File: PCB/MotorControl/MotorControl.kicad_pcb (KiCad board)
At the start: 2 copper layers, 44 x 54.5 mm, 14 parts, among them J1 USB_C_Receptacle_USB2.0_14P, J2 Conn_02x05_Top_Bottom, J3 Conn_01x06, J4 Conn_01x03, SW1 SW_Push, U1 STM32L031K6Tx, U2 TC1262-33

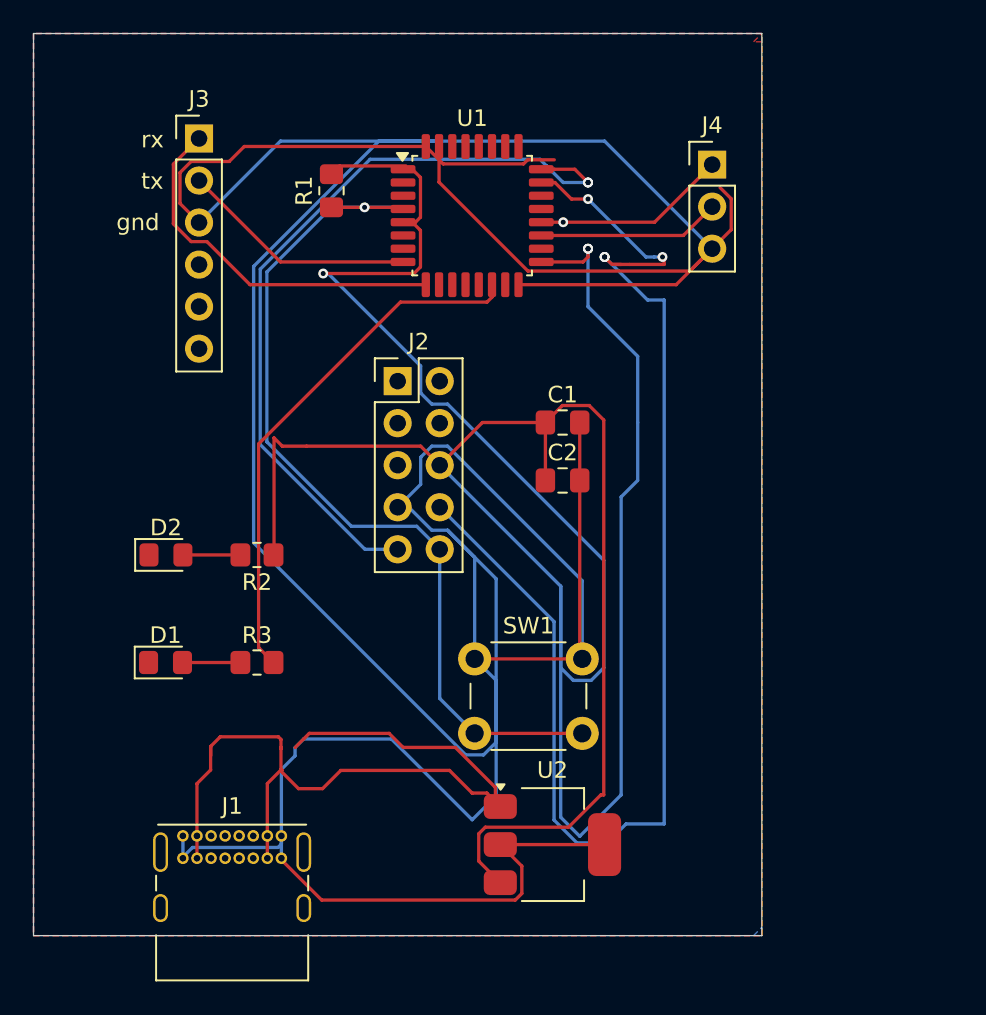
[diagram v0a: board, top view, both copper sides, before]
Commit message: Routing for motor control PCB
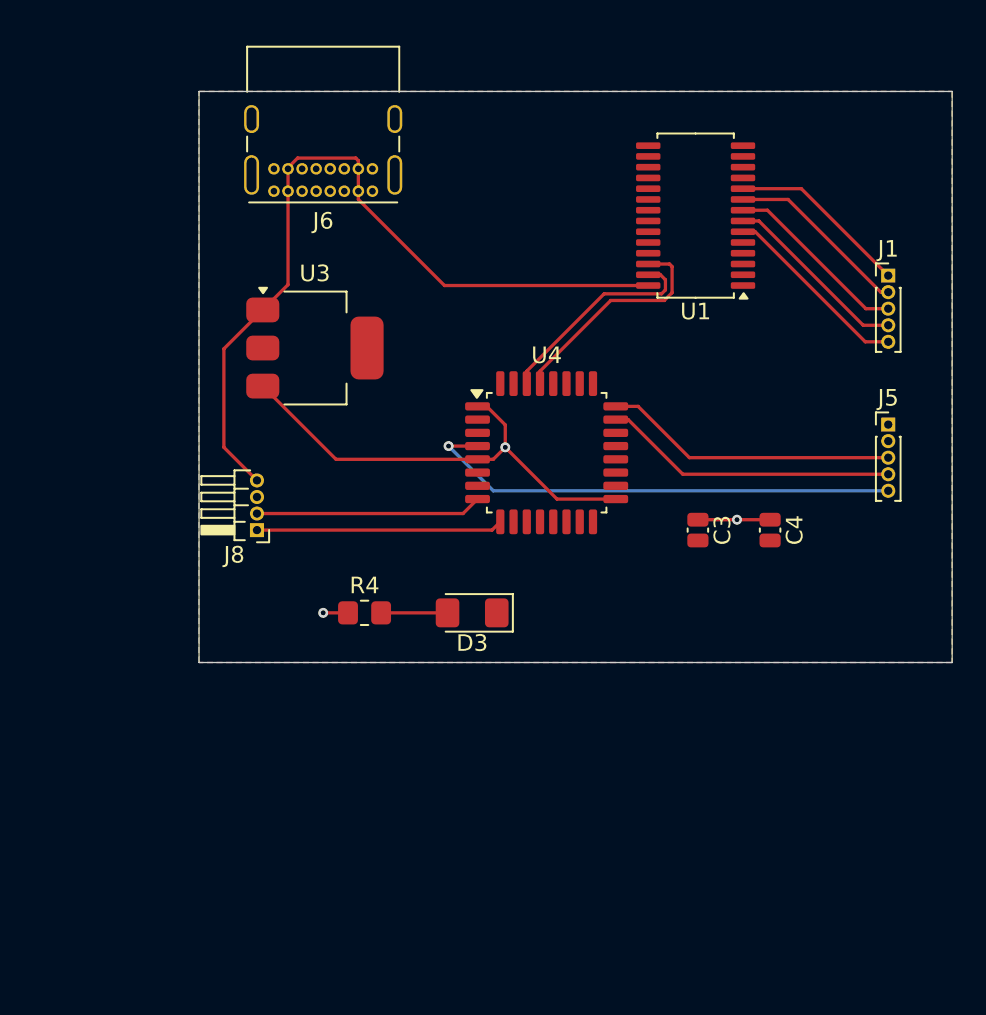
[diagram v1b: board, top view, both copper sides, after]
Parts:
- removed C1: .1uf, Capacitor_SMD:C_0805_2012Metric_Pad1.18x1.45mm_HandSolder
- removed C2: 10uf, Capacitor_SMD:C_0805_2012Metric_Pad1.18x1.45mm_HandSolder
- removed D1, D2: LED, LED_SMD:LED_0805_2012Metric_Pad1.15x1.40mm_HandSolder
- removed J2: Conn_02x05_Top_Bottom, Connector_PinHeader_2.54mm:PinHeader_2x05_P2.54mm_Vertical
- removed J3: Conn_01x06, Connector_PinHeader_2.54mm:PinHeader_1x06_P2.54mm_Vertical
- removed J4: Conn_01x03, Connector_PinHeader_2.54mm:PinHeader_1x03_P2.54mm_Vertical
- removed R1: 4.7k, Resistor_SMD:R_0805_2012Metric_Pad1.20x1.40mm_HandSolder
- removed R2, R3: 330, Resistor_SMD:R_0805_2012Metric_Pad1.20x1.40mm_HandSolder
- removed SW1: SW_Push, Button_Switch_THT:SW_PUSH_6mm_H4.3mm
- removed U2: TC1262-33, Package_TO_SOT_SMD:SOT-223-3_TabPin2
- added C3: 1, Capacitor_SMD:C_0504_1310Metric_Pad0.83x1.28mm_HandSolder, F.Cu at (64.6, 59.0)
- added C4: .1u, Capacitor_SMD:C_0504_1310Metric_Pad0.83x1.28mm_HandSolder, F.Cu at (69.0, 59.0)
- added D3: LED, LED_SMD:LED_1206_3216Metric_Pad1.42x1.75mm_HandSolder, F.Cu at (51.0, 64.0)
- added J5: Conn_01x05_Pin, Connector_PinHeader_1.00mm:PinHeader_1x05_P1.00mm_Vertical, F.Cu at (76.1, 52.6)
- added J6: USB_C_Receptacle_USB2.0_14P, Connector_USB:USB_C_Receptacle_GCT_USB4085, F.Cu at (45.0, 38.5)
- added J8: Conn_01x04_Socket, Connector_PinHeader_1.00mm:PinHeader_1x04_P1.00mm_Horizontal, F.Cu at (38.0, 59.0)
- added R4: 270, Resistor_SMD:R_0805_2012Metric_Pad1.20x1.40mm_HandSolder, F.Cu at (44.5, 64.0)
- added U3: TC1262-33, Package_TO_SOT_SMD:SOT-223-3_TabPin2, F.Cu at (41.5, 48.0)
- added U4: STM32L031K6Tx, Package_QFP:LQFP-32_7x7mm_P0.8mm, F.Cu at (55.5, 54.3)
- J1: value USB_C_Receptacle_USB2.0_14P -> Conn_01x05_Pin; footprint Connector_USB:USB_C_Receptacle_GCT_USB4085 -> Connector_PinHeader_1.00mm:PinHeader_1x05_P1.00mm_Vertical
- U1: value STM32L031K6Tx -> PCA9685PW; footprint Package_QFP:LQFP-32_7x7mm_P0.8mm -> Package_SO:TSSOP-28_4.4x9.7mm_P0.65mm
- moved J1 54.4 mm to (76.1, 43.6)
- moved U1 13.5 mm to (64.5, 40.0), turned to 180 degrees
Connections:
- U1 pad 1: VAPP -> GND
- U1 pad 10: unconnected-(U1-PA4-Pad10) -> Net-(J1-Pin_1)
- U1 pad 14: Net-(U1-PB0) -> GND
- U1 pad 16: GND -> unconnected-(U1-LED9-Pad16)
- U1 pad 17: VAPP -> unconnected-(U1-LED10-Pad17)
- U1 pad 19: SCL -> unconnected-(U1-LED12-Pad19)
- U1 pad 2: unconnected-(U1-PC14-Pad2) -> GND
- U1 pad 20: SDA -> unconnected-(U1-LED13-Pad20)
- U1 pad 23: TMS_SWDIO -> GND
- U1 pad 24: TCK_SWCLK -> GND
- U1 pad 25: unconnected-(U1-PA15-Pad25) -> GND
- U1 pad 26: unconnected-(U1-PB3-Pad26) -> Net-(U1-SCL)
- U1 pad 27: unconnected-(U1-PB4-Pad27) -> Net-(U1-SDA)
- U1 pad 28: unconnected-(U1-PB5-Pad28) -> 5V
- U1 pad 3: unconnected-(U1-PC15-Pad3) -> GND
- U1 pad 4: NRST -> GND
- U1 pad 5: VAPP -> GND
- U1 pad 6: unconnected-(U1-PA0-Pad6) -> Net-(J1-Pin_5)
- U1 pad 7: unconnected-(U1-PA1-Pad7) -> Net-(J1-Pin_4)
- U1 pad 8: tx -> Net-(J1-Pin_3)
- U1 pad 9: rx -> Net-(J1-Pin_2)
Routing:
- net GND: track 286.6 -> 0.00 mm
- net VAPP: track 189.8 -> 0.00 mm, vias 3 -> 0
- net TMS_SWDIO: track 79.7 -> 0.00 mm, vias 4 -> 0
- net +5V: track 49.4 -> 0.00 mm
- net 5V: track 0.00 -> 47.9 mm
- net TCK_SWCLK: track 47.8 -> 0.00 mm, vias 2 -> 0
- net +3.3V: track 0.00 -> 34.1 mm, vias 0 -> 3
- net Net-(U1-PB0): track 32.1 -> 0.00 mm
- net NRST: track 56.0 -> 29.4 mm
- net rx: track 22.6 -> 0.00 mm
- net SWDIO: track 0.00 -> 17.8 mm
- net SWSCLK: track 0.00 -> 17.7 mm
- net RX: track 0.00 -> 14.9 mm
- net tx: track 14.4 -> 0.00 mm
- net Net-(U1-SCL): track 0.00 -> 13.8 mm
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- added copper zone on B.Cu, net +3.3V
- removed copper zone on B.Cu, net VAPP
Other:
- board size 44 x 54.5 mm -> 45.5 x 34.5 mm
- board text removed: "gnd"
- board text removed: "rx"
- board text removed: "tx"

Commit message: Pushing
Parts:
- removed J8: Conn_01x04_Socket, Connector_PinHeader_1.00mm:PinHeader_1x04_P1.00mm_Horizontal
- added J2: Conn_01x03_Pin, Connector_PinHeader_2.54mm:PinHeader_1x03_P2.54mm_Horizontal, F.Cu at (185.0, 56.7)
- added J3: Conn_01x03_Pin, Connector_PinHeader_2.54mm:PinHeader_1x03_P2.54mm_Horizontal, F.Cu at (185.0, 74.4)
- added J4: Conn_01x03_Pin, Connector_PinHeader_2.54mm:PinHeader_1x03_P2.54mm_Horizontal, F.Cu at (185.1, 89.7)
- added J7: Conn_01x03_Pin, Connector_PinHeader_2.54mm:PinHeader_1x03_P2.54mm_Horizontal, F.Cu at (185.0, 102.4)
- added U2: NORA-W106-00B, NORA-W106-00B:XCVR_NORA-W106-00B, F.Cu at (96.9, 96.3)
- J1: value Conn_01x05_Pin -> Conn_01x03_Pin; footprint Connector_PinHeader_1.00mm:PinHeader_1x05_P1.00mm_Vertical -> Connector_PinHeader_2.54mm:PinHeader_1x03_P2.54mm_Horizontal
- moved J1 108.9 mm to (185.0, 41.4)
- moved U1 103.1 mm to (160.7, 77.2)
- moved D3 87.7 mm to (137.8, 51.0), turned to 0 degrees
- moved R4 86.2 mm to (129.7, 51.0)
- moved J5 84.1 mm to (149.9, 93.0)
- moved U4 73.1 mm to (120.6, 87.6)
- moved U3 59.4 mm to (100.4, 55.4), turned to 90 degrees
- moved J6 51.1 mm to (84.4, 70.9), turned to -90 degrees
- moved C4 49.7 mm to (113.9, 80.5), turned to 0 degrees
- moved C3 37.0 mm to (101.4, 63.1), turned to 180 degrees
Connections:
- J1 pad 1: Net-(J1-Pin_1) -> GND
- J1 pad 2: Net-(J1-Pin_2) -> 5V
- U1 pad 10: Net-(J1-Pin_1) -> Net-(J1-Pin_3)
- U1 pad 6: Net-(J1-Pin_5) -> Net-(J7-Pin_3)
- U1 pad 7: Net-(J1-Pin_4) -> Net-(J4-Pin_3)
- U1 pad 8: Net-(J1-Pin_3) -> Net-(J3-Pin_3)
- U1 pad 9: Net-(J1-Pin_2) -> Net-(J2-Pin_3)
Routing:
- net 5V: track 47.9 -> 254.3 mm, vias 0 -> 2
- net Net-(J7-Pin_3): track 0.00 -> 44.7 mm
- net GND: track 0.00 -> 37.8 mm
- net Net-(J4-Pin_3): track 0.00 -> 33.2 mm, vias 0 -> 2
- net Net-(J2-Pin_3): track 0.00 -> 31.4 mm, vias 0 -> 2
- net Net-(J1-Pin_3): track 11.2 -> 42.3 mm, vias 0 -> 2
- net Net-(U1-SDA): track 12.9 -> 41.3 mm, vias 0 -> 2
- net Net-(U1-SCL): track 13.8 -> 40.9 mm
- net Net-(J3-Pin_3): track 0.00 -> 22.9 mm, vias 0 -> 2
- net SWDIO: track 17.8 -> 35.9 mm
- net SWSCLK: track 17.7 -> 35.6 mm
- net +3.3V: track 34.1 -> 17.5 mm, vias 3 -> 7
- net NRST: track 29.4 -> 45.4 mm
- net Net-(D3-A): track 4.01 -> 18.9 mm
- net Net-(J1-Pin_5): track 11.5 -> 0.00 mm
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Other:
- board size 45.5 x 34.5 mm -> 117.9 x 76.4 mm

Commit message: Pushing updated servo controller
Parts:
- added D1: LED, LED_SMD:LED_1206_3216Metric_Pad1.42x1.75mm_HandSolder, F.Cu at (105.3, 103.5)
- added D2: LED, LED_SMD:LED_1206_3216Metric_Pad1.42x1.75mm_HandSolder, F.Cu at (105.4, 108.9)
- added H1: MountingHole_Pad, MountingHole:MountingHole_4.5mm_Pad, F.Cu at (167.3, 47.0)
- added H2: MountingHole_Pad, MountingHole:MountingHole_4.5mm_Pad, F.Cu at (85.3, 89.7)
- added H3: MountingHole_Pad, MountingHole:MountingHole_4.5mm_Pad, F.Cu at (120.2, 64.0)
- added J8: Conn_01x02_Pin, Connector_PinHeader_2.54mm:PinHeader_1x02_P2.54mm_Vertical, F.Cu at (132.2, 103.3)
- added R1: R, Resistor_SMD:R_0805_2012Metric_Pad1.20x1.40mm_HandSolder, F.Cu at (98.3, 103.6)
- added R2: R, Resistor_SMD:R_0805_2012Metric_Pad1.20x1.40mm_HandSolder, F.Cu at (98.2, 109.0)
- J5: footprint Connector_PinHeader_1.00mm:PinHeader_1x05_P1.00mm_Vertical -> Connector_PinHeader_2.54mm:PinHeader_1x05_P2.54mm_Vertical
- moved U2 15.7 mm to (85.3, 106.9)
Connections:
- net Net-(J1-Pin_3) renamed Motor1PWM
- net Net-(U1-SCL) renamed MotorControl_SCL
- U1 pad 28: 5V -> +3.3V
- U2 pad A5: unconnected-(U2-FSPIDQS/GPIO14-PadA5) -> DebugTX
- U2 pad C8: unconnected-(U2-GPIO21-PadC8) -> Switch2
- U2 pad D8: unconnected-(U2-GPIO4-PadD8) -> Switch1
- U2 pad H9: unconnected-(U2-GPIO8-PadH9) -> BlueLED
- U2 pad J3: unconnected-(U2-~{RESET}-PadJ3) -> Net-(U2-~{RESET})
- U2 pad J8: unconnected-(U2-GPIO5-PadJ8) -> RedLED
- U2 pad J9: unconnected-(U2-GPIO3-PadJ9) -> GPIO_J9
- U4 pad 13: unconnected-(U4-PA7-Pad13) -> Net-(U2-~{RESET})
- U4 pad 19: unconnected-(U4-PA9-Pad19) -> Debug_tx
- U4 pad 20: unconnected-(U4-PA10-Pad20) -> Debug_rx
- U4 pad 26: unconnected-(U4-PB3-Pad26) -> GPIO_J9
- U4 pad 27: unconnected-(U4-PB4-Pad27) -> Switch2
- U4 pad 28: unconnected-(U4-PB5-Pad28) -> Switch1
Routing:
- net GPIO_J9: track 0.00 -> 61.8 mm, vias 0 -> 2
- net Net-(U2-~{RESET}): track 0.00 -> 51.7 mm, vias 0 -> 2
- net Switch1: track 0.00 -> 49.1 mm, vias 0 -> 2
- net Switch2: track 0.00 -> 49.1 mm, vias 0 -> 2
- net MotorControl_SCL: track 40.9 -> 69.5 mm, vias 0 -> 3
- net Debug_rx: track 0.00 -> 19.2 mm
- net Debug_tx: track 0.00 -> 17.5 mm
- net 5V: track 254.3 -> 237.7 mm, vias 2 -> 0
- net RX: track 21.3 -> 37.4 mm, vias 0 -> 2
- net Motor1PWM: track 42.3 -> 57.1 mm
- net TX: track 17.3 -> 30.1 mm
- net RedLED: track 0.00 -> 12.1 mm, vias 0 -> 2
- net BlueLED: track 0.00 -> 11.8 mm, vias 0 -> 2
- net GND: track 37.8 -> 26.6 mm
- net DebugTX: track 0.00 -> 10.8 mm
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
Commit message: Motor
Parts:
- removed D2: LED, LED_SMD:LED_1206_3216Metric_Pad1.42x1.75mm_HandSolder
- removed H1, H2, H3: MountingHole_Pad, MountingHole:MountingHole_4.5mm_Pad
- removed J8: Conn_01x02_Pin, Connector_PinHeader_2.54mm:PinHeader_1x02_P2.54mm_Vertical
- removed R1: R, Resistor_SMD:R_0805_2012Metric_Pad1.20x1.40mm_HandSolder
- added J9: Conn_01x06_Socket, Connector_PinSocket_2.54mm:PinSocket_1x06_P2.54mm_Vertical, F.Cu at (139.8, 103.2)
- added TP1: TestPoint, TestPoint:TestPoint_Pad_2.5x2.5mm, F.Cu at (120.4, 64.0)
- added TP2: TestPoint, TestPoint:TestPoint_Pad_2.5x2.5mm, F.Cu at (177.6, 53.8)
- added TP3: TestPoint, TestPoint:TestPoint_Pad_2.5x2.5mm, F.Cu at (85.5, 90.3)
- D1: value LED -> ASMB-MTB0-0A3A2; footprint LED_SMD:LED_1206_3216Metric_Pad1.42x1.75mm_HandSolder -> LED_SMD:LED_Avago_PLCC4_3.2x2.8mm_CW
- moved J5 4.15 mm to (149.9, 88.9)
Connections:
- net NRST renamed Net-(J5-Pin_5)
- D1 pad 1: GND -> Net-(D1-A)
- D1 pad 2: Net-(D1-A) -> BlueLED
- R2 pad 1: Net-(D2-A) -> GND
- R2 pad 2: RedLED -> Net-(D1-A)
- U4 pad 19: Debug_tx -> Debug_rx
- U4 pad 20: Debug_rx -> Debug_tx
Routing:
- net RedLED: track 12.1 -> 25.9 mm
- net Motor1PWM: track 57.1 -> 47.2 mm
- net Net-(D1-A): track 4.63 -> 11.6 mm
- net SWSCLK: track 35.6 -> 28.9 mm
- net SWDIO: track 35.9 -> 29.7 mm
- net Net-(D2-A): track 4.75 -> 0.00 mm
- net BlueLED: track 11.8 -> 15.8 mm, vias 2 -> 0
- net 5V: track 237.7 -> 234.6 mm
- net Debug_tx: track 17.5 -> 19.2 mm
- net Debug_rx: track 19.2 -> 17.5 mm
- net Net-(J5-Pin_5): track 45.4 -> 46.3 mm

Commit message: wasd
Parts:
- added C1: C, Capacitor_SMD:C_0504_1310Metric_Pad0.83x1.28mm_HandSolder, F.Cu at (127.3, 92.6)
- added C2: C, Capacitor_SMD:C_0504_1310Metric_Pad0.83x1.28mm_HandSolder, F.Cu at (110.7, 87.9)
- added C5: C, Capacitor_SMD:C_0504_1310Metric_Pad0.83x1.28mm_HandSolder, F.Cu at (86.9, 95.9)
- added C6: C, Capacitor_SMD:C_0504_1310Metric_Pad0.83x1.28mm_HandSolder, F.Cu at (92.5, 98.6)
- added C7: C, Capacitor_SMD:C_0504_1310Metric_Pad0.83x1.28mm_HandSolder, F.Cu at (89.9, 96.0)
- added D2: LED, LED_SMD:LED_1206_3216Metric_Pad1.42x1.75mm_HandSolder, F.Cu at (122.7, 108.0)
- added R1: 270, Resistor_SMD:R_0805_2012Metric_Pad1.20x1.40mm_HandSolder, F.Cu at (122.7, 102.1)
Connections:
- net Net-(J5-Pin_5) renamed NRST
- D1 pad 3: unconnected-(D1-GK-Pad3) -> GreenLED
- U2 pad A7: unconnected-(U2-VCCIO-PadA7)_1 -> +3.3V
- U2 pad B7: unconnected-(U2-VCCIO-PadA7) -> +3.3V
- U2 pad F8: unconnected-(U2-GPIO45-PadF8) -> UART_RTS->Board_CTS
- U2 pad F9: unconnected-(U2-GPIO6-PadF9) -> UART_CTS->Board_RTS
- U2 pad G8: TX -> RX
- U2 pad G9: RX -> TX
- U2 pad H8: unconnected-(U2-GPIO2-PadH8) -> GreenLED
- U4 pad 14: unconnected-(U4-PB0-Pad14) -> UART_CTS->Board_RTS
- U4 pad 15: unconnected-(U4-PB1-Pad15) -> HeartBeat
- U4 pad 21: unconnected-(U4-PA11-Pad21) -> UART_RTS->Board_CTS
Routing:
- net UART_RTS->Board_CTS: track 0.00 -> 65.8 mm, vias 0 -> 4
- net UART_CTS->Board_RTS: track 0.00 -> 42.4 mm
- net GreenLED: track 0.00 -> 21.3 mm, vias 0 -> 2
- net +3.3V: track 23.0 -> 40.1 mm
- net HeartBeat: track 0.00 -> 9.35 mm
- net RX: track 37.4 -> 44.1 mm
- net GPIO_J9: track 61.8 -> 65.4 mm
- net Net-(D2-A): track 0.00 -> 3.37 mm
- net TX: track 30.1 -> 30.9 mm
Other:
- board text added: "3.3v"
- board text added: "Debug_TX"
- board text added: "PWMControllerSDA"
- board text added: "Servo1PWM"
- board text added: "gnd"
- board text added: "nrst"
- board text added: "rx"
- board text added: "swdio"
- board text added: "swsclk"
- board text added: "tx"

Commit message: Thing
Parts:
- moved C6 6.08 mm to (93.0, 92.5), turned to 90 degrees
- moved C7 3.32 mm to (93.0, 97.2)
- moved C5 2.46 mm to (88.6, 94.1)
- moved U2 0.09 mm to (85.3, 106.8)
- turned D3 to 180 degrees
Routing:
- net Net-(D3-A): track 18.9 -> 5.58 mm
- net 5V: track 234.6 -> 227.9 mm
- net Net-(U2-~{RESET}): track 51.7 -> 57.5 mm, vias 2 -> 3
- net GreenLED: track 21.3 -> 17.5 mm
- net +3.3V: track 40.1 -> 43.5 mm
- net TX: track 30.9 -> 33.7 mm
- net RX: track 44.1 -> 44.6 mm

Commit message: Updated Motor Control
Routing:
- net GND: track 26.6 -> 7.38 mm
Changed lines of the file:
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@@
 		(sheetname "/")
 		(sheetfile "MotorControl.kicad_sch")
+		(clearance 0.15)
 		(attr smd)
 		(fp_line
@@
 	)
 	(segment
-		(start 83.693 107.0288)
-		(end 84.7334 105.9884)
-		(width 0.2)
-		(layer "F.Cu")
-		(net 2)
-	)
-	(segment
-		(start 83.693 109.7788)
-		(end 83.693 107.0288)
-		(width 0.2)
-		(layer "F.Cu")
-		(net 2)
-	)
-	(segment
-		(start 81.9834 101.5884)
-		(end 80.8834 100.4884)
-		(width 0.2)
-		(layer "F.Cu")
-		(net 2)
-	)
-	(segment
-		(start 83.0834 110.3884)
-		(end 83.693 109.7788)
-		(width 0.2)
-		(layer "F.Cu")
-		(net 2)
-	)
-	(segment
 		(start 100.4183 62.6843)
 		(end 100.8022 63.0682)
@@
 	)
 	(segment
-		(start 88.5834 110.3884)
-		(end 81.9834 110.3884)
-		(width 0.2)
-		(layer "F.Cu")
-		(net 2)
-	)
-	(segment
-		(start 88.5834 101.5884)
-		(end 89.6834 100.4884)
-		(width 0.2)
-		(layer "F.Cu")
-		(net 2)
-	)
-	(segment
 		(start 84.4414 70.939)
 		(end 83.0914 70.939)
@@
 	)
 	(segment
-		(start 84.7334 104.8884)
-		(end 84.7334 104.3384)
-		(width 0.2)
-		(layer "F.Cu")
-		(net 2)
-	)
-	(segment
-		(start 84.7334 104.3384)
-		(end 81.9834 101.5884)
-		(width 0.2)
-		(layer "F.Cu")
-		(net 2)
-	)
-	(segment
 		(start 84.4414 76.889)
 		(end 83.0914 76.889)
@@
 		(layer "F.Cu")
 		(hatch edge 0.5)
-		(connect_pads
+		(connect_pads yes
 			(clearance 0.5)
 		)
